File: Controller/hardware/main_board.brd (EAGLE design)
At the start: 75 x 59 mm, 47 parts, among them IC1 LINEAR_78DT, IC2 40XX_4050D, IC3 LP298XS, IC5 ATMEGA328, U1 CSTNE16M0VH3L000R0, X1 MICROSD_SMD, X4 CON-PHOENIX-508_MST2V

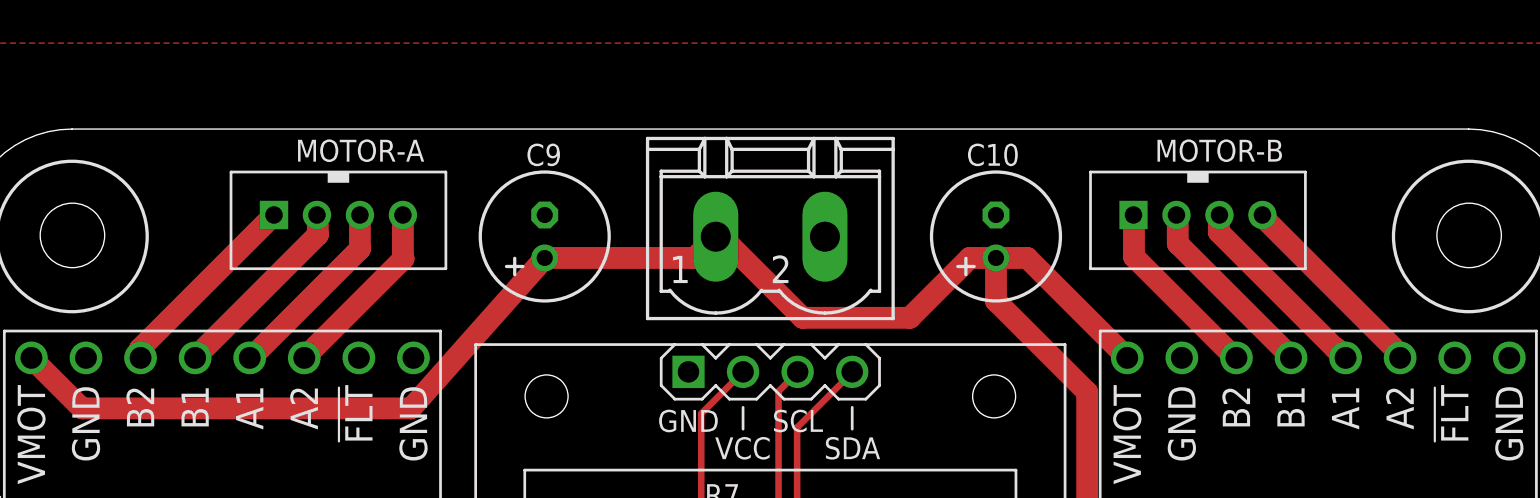
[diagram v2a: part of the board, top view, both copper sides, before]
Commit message: changed motor connectors
changed motor connectors to .1" pitch 4 pos headers. the stepper motor stock connectors press nicely onto these. so if one wanted to they could just pins instead of soldering wires directly to the board. if soldering directly to the board the new larger pads should be more robust too.
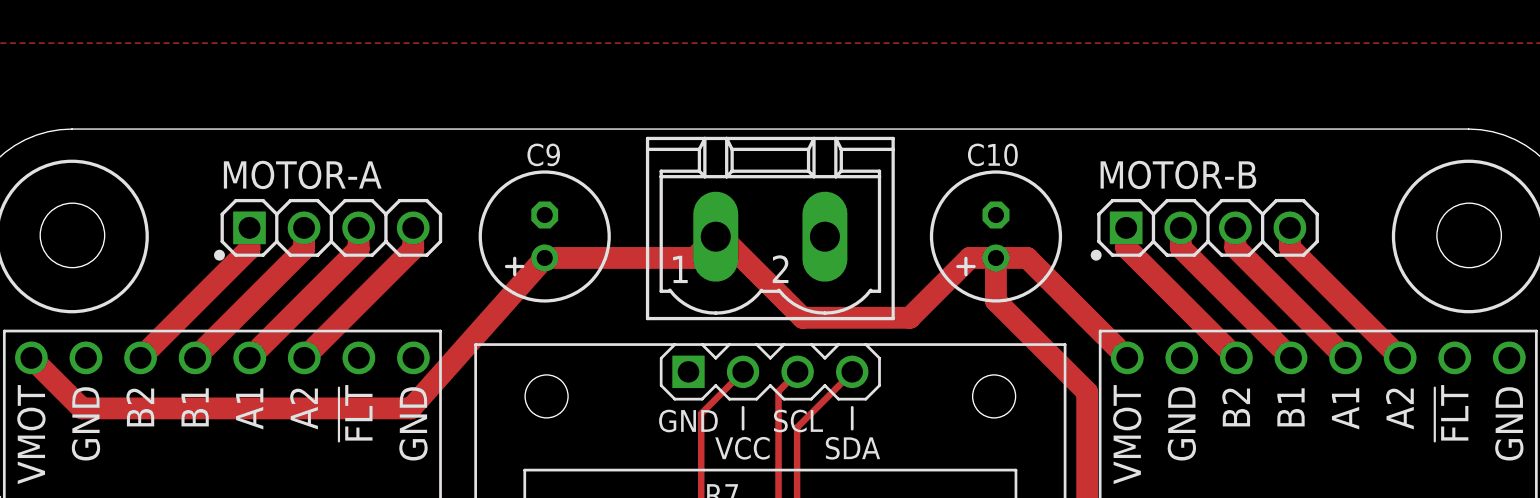
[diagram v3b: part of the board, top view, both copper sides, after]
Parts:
- MOTOR-A, MOTOR-B: value JST_EPH_4PIN -> (none); device main_board:JST_EPH_B4B-PH-K-S -> main_board:1X04
- moved MOTOR-A 1.71 mm to (15.8, 54.4), turned to 0 degrees
- moved MOTOR-B 1.00 mm to (56.6, 54.4), turned to 0 degrees
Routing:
- net N$19: track 9.75 -> 8.17 mm
- net N$21: track 9.30 -> 8.17 mm
- net N$13: track 9.25 -> 8.15 mm
- net N$14: track 9.04 -> 8.15 mm
- net N$18: track 8.85 -> 8.17 mm
- net N$15: track 8.81 -> 8.15 mm
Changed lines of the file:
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@@
 <attribute name="VENDOR_PN" value="1189-1148-ND" x="48" y="54" size="1.778" layer="27" rot="R90" display="off"/>
-</element>
-<element name="MOTOR-A" library="main_board" package="JST_EPH_B4B-PH-K-S" value="JST_EPH_4PIN" x="17.4" y="55" smashed="yes" rot="R180">
-<attribute name="NAME" x="21.4" y="58.5" size="1.016" layer="25" rot="R180"/>
-</element>
-<element name="MOTOR-B" library="main_board" package="JST_EPH_B4B-PH-K-S" value="JST_EPH_4PIN" x="57.4" y="55" smashed="yes" rot="R180">
-<attribute name="NAME" x="61.4" y="58.5" size="1.016" layer="25" rot="R180"/>
 </element>
 <element name="J1" library="main_board" package="JUMPER_05C" value="" x="35" y="2" smashed="yes">
@@
 <attribute name="VENDOR" value="digikey" x="22" y="4" size="1.778" layer="27" display="off"/>
 <attribute name="VENDOR_PN" value="1276-6471-1-ND" x="22" y="4" size="1.778" layer="27" display="off"/>
+</element>
+<element name="MOTOR-A" library="main_board" package="1X04" value="" x="15.8" y="54.4" smashed="yes">
+<attribute name="NAME" x="11.9138" y="56.2288" size="1.27" layer="25" ratio="10"/>
+<attribute name="VALUE" x="11.99" y="51.225" size="1.27" layer="27"/>
+</element>
+<element name="MOTOR-B" library="main_board" package="1X04" value="" x="56.6" y="54.4" smashed="yes">
+<attribute name="NAME" x="52.7138" y="56.2288" size="1.27" layer="25" ratio="10"/>
+<attribute name="VALUE" x="52.79" y="51.225" size="1.27" layer="27"/>
 </element>
 </elements>
@@
 <contactref element="IC_A_MOTOR" pad="14"/>
 <contactref element="MOTOR-A" pad="1"/>
-<wire x1="8.1568" y1="48.76825" x2="14.37456875" y2="54.98601875" width="1.016" layer="1"/>
-<wire x1="8.1568" y1="48.431" x2="8.1568" y2="48.76825" width="1.016" layer="1"/>
-<wire x1="14.37456875" y1="54.98601875" x2="14.4" y2="55" width="1.016" layer="1"/>
-<wire x1="8.1568" y1="48.431" x2="8.19" y2="48.35" width="0.6096" layer="1"/>
+<wire x1="8.19" y1="48.35" x2="13.26" y2="53.42" width="1.016" layer="1"/>
+<wire x1="13.26" y1="53.42" x2="13.26" y2="54.4" width="1.016" layer="1"/>
 </signal>
 <signal name="N$14" class="1">
 <contactref element="IC_A_MOTOR" pad="13"/>
 <contactref element="MOTOR-A" pad="2"/>
-<wire x1="16.44105" y1="54.07605" x2="16.44105" y2="54.93095" width="1.016" layer="1"/>
-<wire x1="10.72655" y1="48.36155" x2="16.44105" y2="54.07605" width="1.016" layer="1"/>
-<wire x1="10.73" y1="48.35" x2="10.72655" y2="48.35345" width="1.016" layer="1"/>
-<wire x1="10.72655" y1="48.35345" x2="10.72655" y2="48.36155" width="1.016" layer="1"/>
-<wire x1="16.4" y1="55" x2="16.44105" y2="54.95895" width="1.016" layer="1"/>
-<wire x1="16.44105" y1="54.95895" x2="16.44105" y2="54.93095" width="1.016" layer="1"/>
+<wire x1="10.73" y1="48.35" x2="15.8" y2="53.42" width="1.016" layer="1"/>
+<wire x1="15.8" y1="53.42" x2="15.8" y2="54.4" width="1.016" layer="1"/>
 </signal>
 <signal name="N$15" class="1">
 <contactref element="IC_A_MOTOR" pad="12"/>
 <contactref element="MOTOR-A" pad="3"/>
-<wire x1="18.4" y1="55" x2="18.4" y2="53.41775" width="1.016" layer="1"/>
-<wire x1="13.27" y1="48.35" x2="13.33225" y2="48.35" width="1.016" layer="1"/>
-<wire x1="18.4" y1="53.41775" x2="13.33225" y2="48.35" width="1.016" layer="1"/>
+<wire x1="13.27" y1="48.35" x2="18.34" y2="53.42" width="1.016" layer="1"/>
+<wire x1="18.34" y1="53.42" x2="18.34" y2="54.4" width="1.016" layer="1"/>
 </signal>
 <signal name="N$16" class="1">
 <contactref element="IC_A_MOTOR" pad="11"/>
 <contactref element="MOTOR-A" pad="4"/>
-<wire x1="20.43" y1="52.97" x2="20.4" y2="53" width="1.016" layer="1"/>
-<wire x1="20.4" y1="55" x2="20.4" y2="53" width="1.016" layer="1"/>
-<wire x1="15.81" y1="48.35" x2="20.43" y2="52.97" width="1.016" layer="1"/>
+<wire x1="15.81" y1="48.35" x2="20.88" y2="53.42" width="1.016" layer="1"/>
+<wire x1="20.88" y1="53.42" x2="20.88" y2="54.4" width="1.016" layer="1"/>
 </signal>
 <signal name="N$17" class="1">
 <contactref element="IC_B_MOTOR" pad="14"/>
 <contactref element="MOTOR-B" pad="1"/>
-<wire x1="54.42115" y1="53.05645" x2="54.42115" y2="54.93095" width="1.016" layer="1"/>
-<wire x1="59.19" y1="48.35" x2="59.1276" y2="48.35" width="1.016" layer="1"/>
-<wire x1="59.1276" y1="48.35" x2="54.42115" y2="53.05645" width="1.016" layer="1"/>
-<wire x1="54.42115" y1="54.93095" x2="54.4" y2="55" width="0.6096" layer="1"/>
+<wire x1="59.19" y1="48.35" x2="54.06" y2="53.48" width="1.016" layer="1"/>
+<wire x1="54.06" y1="53.48" x2="54.06" y2="54.4" width="1.016" layer="1"/>
 </signal>
 <signal name="N$18" class="1">
 <contactref element="IC_B_MOTOR" pad="13"/>
 <contactref element="MOTOR-B" pad="2"/>
-<wire x1="61.6858" y1="48.4408" x2="56.46035" y2="53.66625" width="1.016" layer="1"/>
-<wire x1="56.46035" y1="53.66625" x2="56.46035" y2="54.93095" width="1.016" layer="1"/>
-<wire x1="61.6858" y1="48.431" x2="61.6858" y2="48.4408" width="1.016" layer="1"/>
-<wire x1="56.46035" y1="54.93095" x2="56.4" y2="55" width="1.016" layer="1"/>
-<wire x1="61.6858" y1="48.431" x2="61.73" y2="48.35" width="1.016" layer="1"/>
+<wire x1="61.73" y1="48.35" x2="56.6" y2="53.48" width="1.016" layer="1"/>
+<wire x1="56.6" y1="53.48" x2="56.6" y2="54.4" width="1.016" layer="1"/>
 </signal>
 <signal name="N$19" class="1">
 <contactref element="IC_B_MOTOR" pad="12"/>
 <contactref element="MOTOR-B" pad="3"/>
-<wire x1="58.3721" y1="54.2035" x2="58.3721" y2="54.93095" width="1.016" layer="1"/>
-<wire x1="64.2256" y1="48.35" x2="63.7878" y2="48.7878" width="1.016" layer="1"/>
-<wire x1="63.7878" y1="48.7878" x2="58.3721" y2="54.2035" width="1.016" layer="1"/>
-<wire x1="63.7878" y1="48.7878" x2="63.8322" y2="48.7878" width="1.016" layer="1"/>
-<wire x1="63.8322" y1="48.7878" x2="64.27" y2="48.35" width="1.016" layer="1"/>
-<wire x1="58.4" y1="55" x2="58.3721" y2="54.9721" width="1.016" layer="1"/>
-<wire x1="58.3721" y1="54.9721" x2="58.3721" y2="54.93095" width="1.016" layer="1"/>
+<wire x1="64.27" y1="48.35" x2="59.14" y2="53.48" width="1.016" layer="1"/>
+<wire x1="59.14" y1="53.48" x2="59.14" y2="54.4" width="1.016" layer="1"/>
 </signal>
 <signal name="N$21" class="1">
 <contactref element="IC_B_MOTOR" pad="11"/>
 <contactref element="MOTOR-B" pad="4"/>
-<wire x1="66.7838" y1="48.5408" x2="60.4" y2="54.9246" width="1.016" layer="1"/>
-<wire x1="60.4" y1="55" x2="60.4" y2="54.9246" width="1.016" layer="1"/>
-<wire x1="66.7838" y1="48.431" x2="66.7838" y2="48.5408" width="1.016" layer="1"/>
-<wire x1="66.7838" y1="48.431" x2="66.81" y2="48.35" width="1.016" layer="1"/>
+<wire x1="66.81" y1="48.35" x2="61.68" y2="53.48" width="1.016" layer="1"/>
+<wire x1="61.68" y1="53.48" x2="61.68" y2="54.4" width="1.016" layer="1"/>
 </signal>
 <signal name="N$22">
